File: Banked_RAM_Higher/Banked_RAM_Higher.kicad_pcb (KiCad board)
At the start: 2 copper layers, 50.8 x 104.1 mm, 19 parts, among them J1 Bus_Wide, J2 Conn_02x08_Odd_Even, J3 Conn_02x03_Odd_Even, U1 74LS32, U2 74LS04, U3 74LS138, U4 AS6C4008-55PCN, U5 74LS273

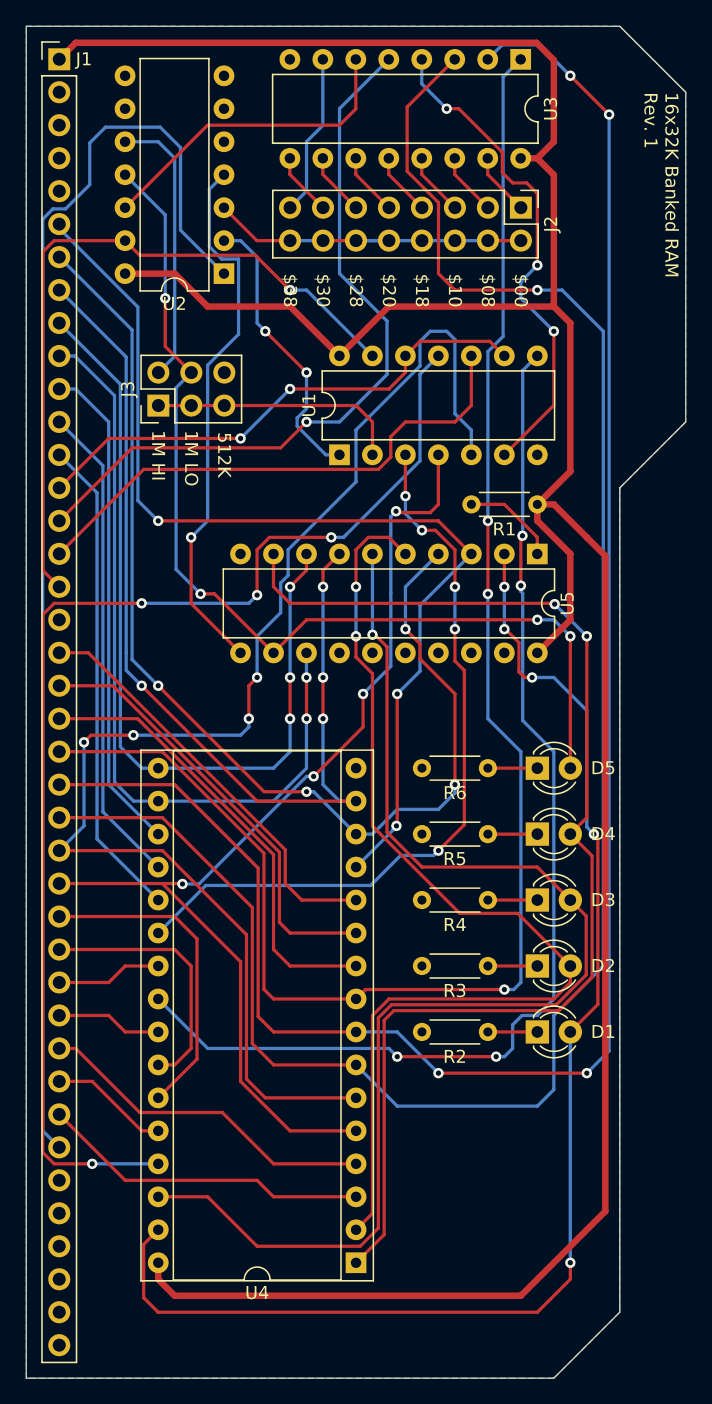
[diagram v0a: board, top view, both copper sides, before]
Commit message: Updating schematic and PCBs for banked ram and timer
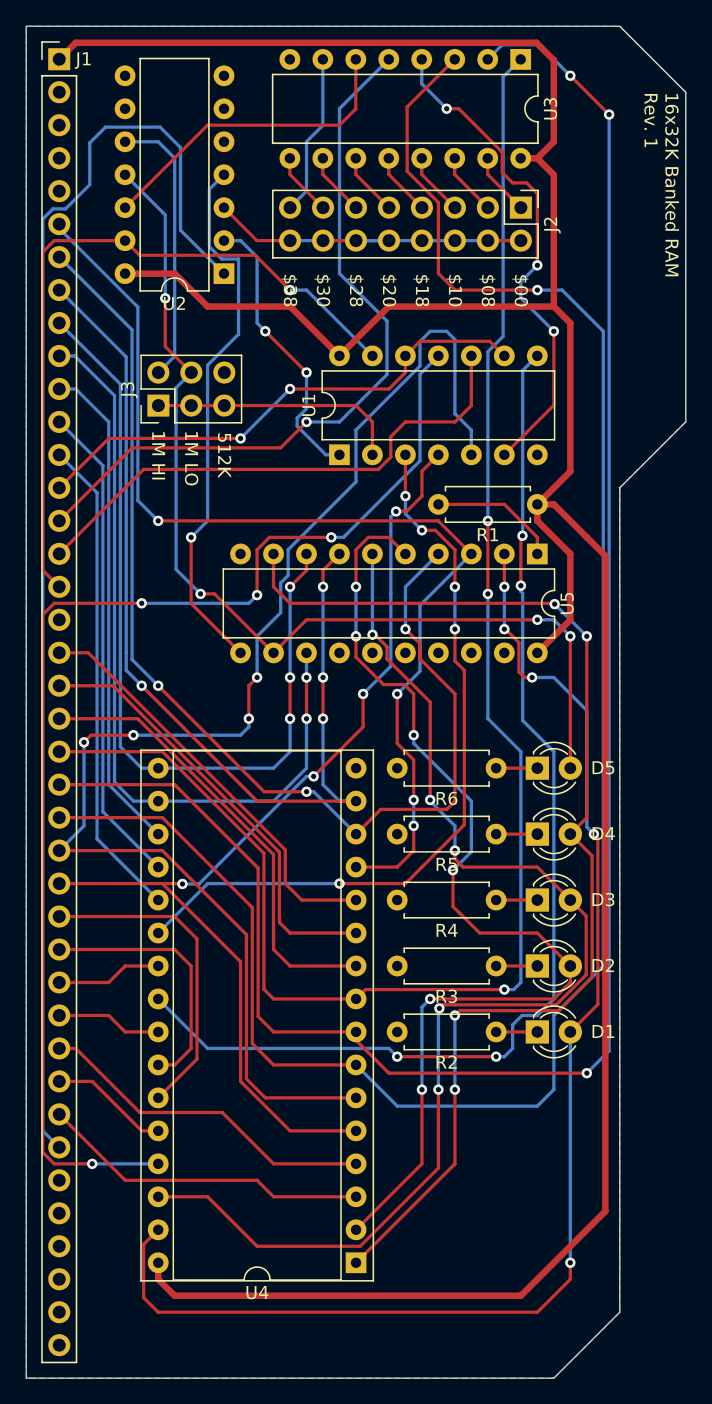
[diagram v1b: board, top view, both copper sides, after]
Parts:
- R1, R2, R3, R4, R5, R6: footprint Resistor_THT:R_Axial_DIN0204_L3.6mm_D1.6mm_P5.08mm_Horizontal -> Resistor_THT:R_Axial_DIN0207_L6.3mm_D2.5mm_P7.62mm_Horizontal
- moved R2 0.64 mm to (125.1, 115.6)
- moved R3 0.64 mm to (125.1, 110.5)
- moved R4 0.64 mm to (125.1, 105.4)
- moved R5 0.64 mm to (125.1, 100.3)
- moved R6 0.64 mm to (125.1, 95.2)
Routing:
- net BANK2: track 97.3 -> 93.1 mm, vias 1 -> 5
- net BANK3: track 92.7 -> 89.7 mm, vias 2 -> 4
- net D0: track 79.2 -> 81.9 mm, vias 3 -> 4
- net Net-(R1-Pad2): track 7.41 -> 9.95 mm
- net A7: track 81.7 -> 80.5 mm
- net Net-(D5-Pad1): track 3.81 -> 3.18 mm
- net Net-(D4-Pad1): track 3.81 -> 3.18 mm
- net Net-(D3-Pad1): track 3.81 -> 3.18 mm
- net Net-(D2-Pad1): track 3.81 -> 3.18 mm
- net Net-(D1-Pad1): track 3.81 -> 3.18 mm
- net GND: track 0.00 -> 0.61 mm
- net A4: track 143.1 -> 143.5 mm, vias 4 -> 3
- net D1: track 86.1 -> 86.5 mm, vias 4 -> 3
- net BANK1: track 80.8 -> 81.1 mm, vias 2 -> 6
